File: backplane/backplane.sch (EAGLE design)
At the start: 4 parts

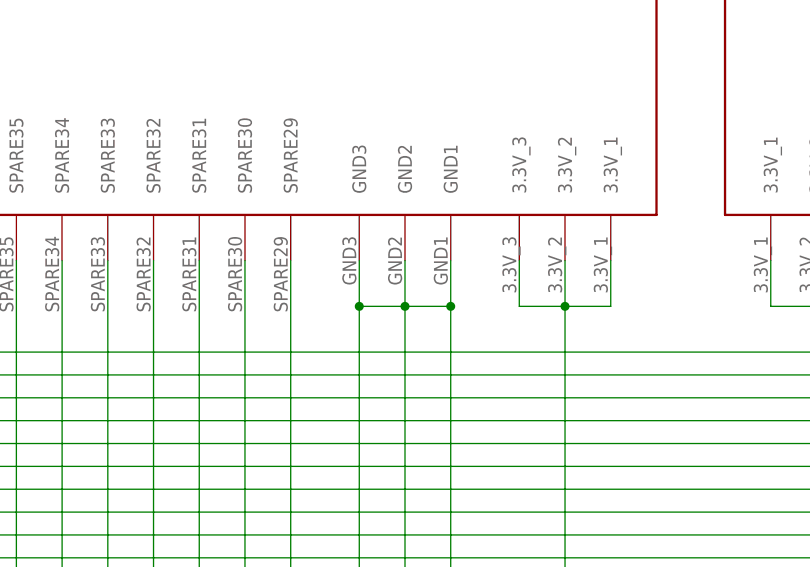
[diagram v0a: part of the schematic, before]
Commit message: Updated backplane with all topside traces, correct planes.
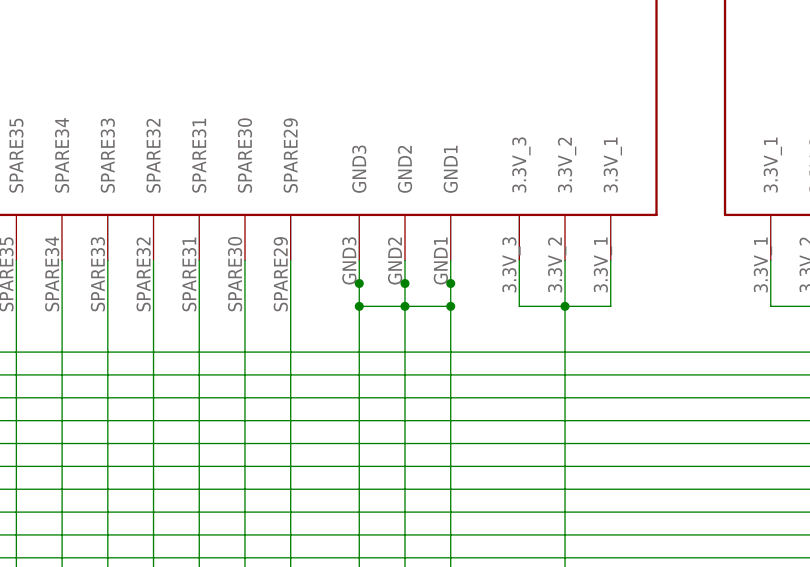
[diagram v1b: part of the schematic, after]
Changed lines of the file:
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@@
 <segment>
 <pinref part="LOAD_BALANCER" gate="G$1" pin="GND1"/>
-<wire x1="121.92" y1="-33.02" x2="121.92" y2="-38.1" width="0.1524" layer="91"/>
+<wire x1="121.92" y1="-33.02" x2="121.92" y2="-35.56" width="0.1524" layer="91"/>
 <pinref part="CO-PROCESSOR" gate="G$1" pin="GND1"/>
+<wire x1="121.92" y1="-35.56" x2="121.92" y2="-38.1" width="0.1524" layer="91"/>
 <wire x1="121.92" y1="-38.1" x2="121.92" y2="-104.14" width="0.1524" layer="91"/>
 <wire x1="121.92" y1="-104.14" x2="-48.26" y2="-104.14" width="0.1524" layer="91"/>
@@
 <pinref part="LOAD_BALANCER" gate="G$1" pin="GND2"/>
 <wire x1="-48.26" y1="-38.1" x2="-48.26" y2="-33.02" width="0.1524" layer="91"/>
-<wire x1="116.84" y1="-33.02" x2="116.84" y2="-38.1" width="0.1524" layer="91"/>
+<wire x1="116.84" y1="-33.02" x2="116.84" y2="-35.56" width="0.1524" layer="91"/>
 <pinref part="CO-PROCESSOR" gate="G$1" pin="GND2"/>
+<wire x1="116.84" y1="-35.56" x2="116.84" y2="-38.1" width="0.1524" layer="91"/>
 <wire x1="116.84" y1="-38.1" x2="116.84" y2="-101.6" width="0.1524" layer="91"/>
 <wire x1="116.84" y1="-101.6" x2="-53.34" y2="-101.6" width="0.1524" layer="91"/>
@@
 <wire x1="-58.42" y1="-99.06" x2="111.76" y2="-99.06" width="0.1524" layer="91"/>
 <wire x1="111.76" y1="-99.06" x2="111.76" y2="-38.1" width="0.1524" layer="91"/>
-<wire x1="111.76" y1="-38.1" x2="111.76" y2="-33.02" width="0.1524" layer="91"/>
+<wire x1="111.76" y1="-38.1" x2="111.76" y2="-35.56" width="0.1524" layer="91"/>
+<wire x1="111.76" y1="-35.56" x2="111.76" y2="-33.02" width="0.1524" layer="91"/>
 <wire x1="-53.34" y1="-38.1" x2="-58.42" y2="-38.1" width="0.1524" layer="91"/>
 <junction x="-58.42" y="-38.1"/>
@@
 <junction x="111.76" y="-99.06"/>
 <junction x="185.42" y="-99.06"/>
+<junction x="121.92" y="-35.56"/>
+<junction x="116.84" y="-35.56"/>
+<junction x="111.76" y="-35.56"/>
 </segment>
 <segment>
